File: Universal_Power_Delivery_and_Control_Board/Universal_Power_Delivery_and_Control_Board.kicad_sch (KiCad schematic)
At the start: 25 parts, among them SW2 TS1102-TD35HBM, U17 SN74LVC1G17DCKR, U19 TF-0803-0, U20 TCA9555PWR, U22 HC-PM254-8.5H-2X4PW-02A

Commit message: Fished layout for now, need to add some components for optional functionality.
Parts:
- removed C35, C36, C47: 100nF, Capacitor_SMD:C_0402_1005Metric_Pad0.74x0.62mm_HandSolder, symbol Device:C
- removed JP5, JP6: SolderJumper_3_Bridged12, Jumper:SolderJumper-3_P1.3mm_Bridged12_Pad1.0x1.5mm_NumberLabels, symbol Jumper:SolderJumper_3_Bridged12
- removed LED3: SK6812SIDE-A_C5378721, lcsc_footprints:C5378721_LED-SMD_4P-L4_0-W1_6-L, symbol lcsc_imported:SK6812SIDE-A_C5378721
- removed R29: 470R, Resistor_SMD:R_0402_1005Metric_Pad0.72x0.64mm_HandSolder, symbol Device:R
- removed R39: 100K, Resistor_SMD:R_0402_1005Metric_Pad0.72x0.64mm_HandSolder, symbol Device:R
- removed R40: 10K, Resistor_SMD:R_0402_1005Metric_Pad0.72x0.64mm_HandSolder, symbol Device:R
- removed SW2: TS1102-TD35HBM, lcsc_footprints:C36936640_SW-SMD_TS1102-TD35HBM, symbol lcsc_imported:TS1102-TD35HBM
- removed U17: SN74LVC1G17DCKR, lcsc_footprints:C10425_SC-70-5_L2_1-W1_3-P0_65-LS2_1-BR, symbol lcsc_imported:SN74LVC1G17DCKR
- added H1, H2, H3, H4: MountingHole_Pad, MountingHole:MountingHole_2.2mm_M2_Pad_Via, symbol Mechanical:MountingHole_Pad
- added R45: 33R, Resistor_SMD:R_0402_1005Metric_Pad0.72x0.64mm_HandSolder, symbol Device:R
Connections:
- net GND: now also U20.2 (A1), U20.3 (A2), H1.1, H2.1, H3.1, H4.1
- net P06: now reaches U20.10 (P06)
- net P07: now reaches U20.11 (P07)
- net at A1.5 (GPIO3): now also R45.2
- net PD_Section/IND_LED_DIN renamed UI_Section/IND_LED_DIN
- new net Button_LED_DIN: R45.1
- no-connect marks 9 -> 7
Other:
- added sheet UI_Section (UI_Section.kicad_sch)
- sheet PD_Section ports: added none; removed IND_LED_DIN, IND_LED_DOUT
- moved on the sheet: A1, C37, C38, C42, C43, R19, R20, R21, R25, R26, R30, U19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

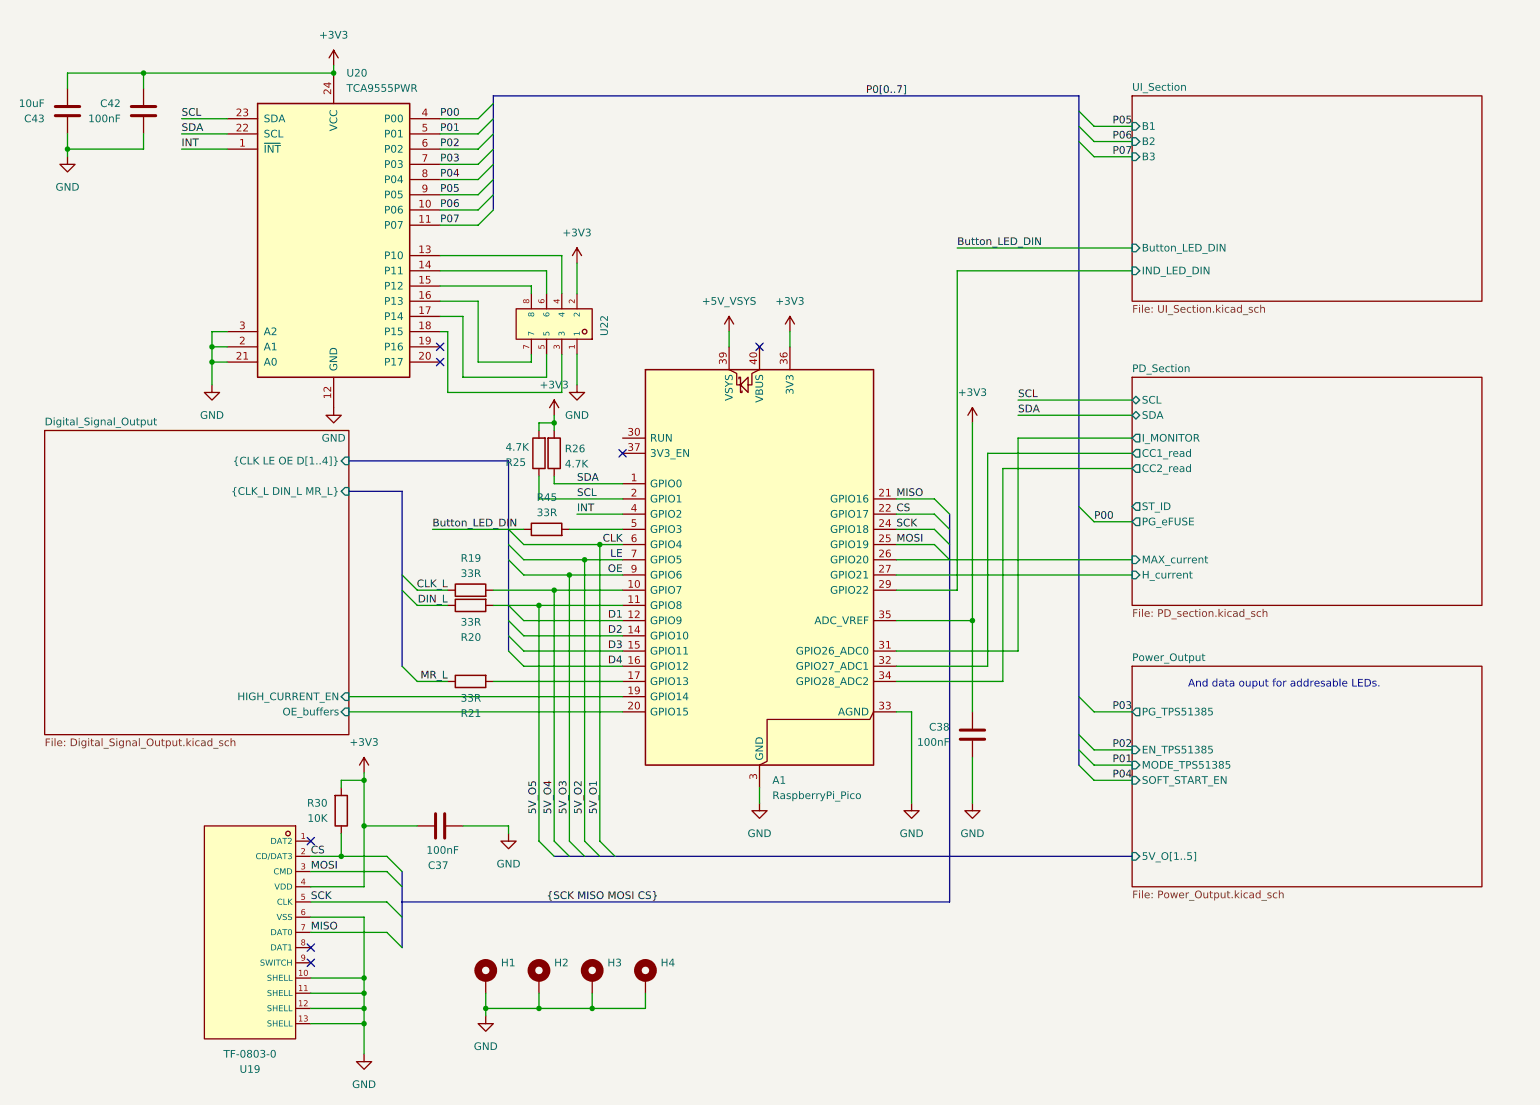
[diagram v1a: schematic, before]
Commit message: Finished layout 0 DRC errors.
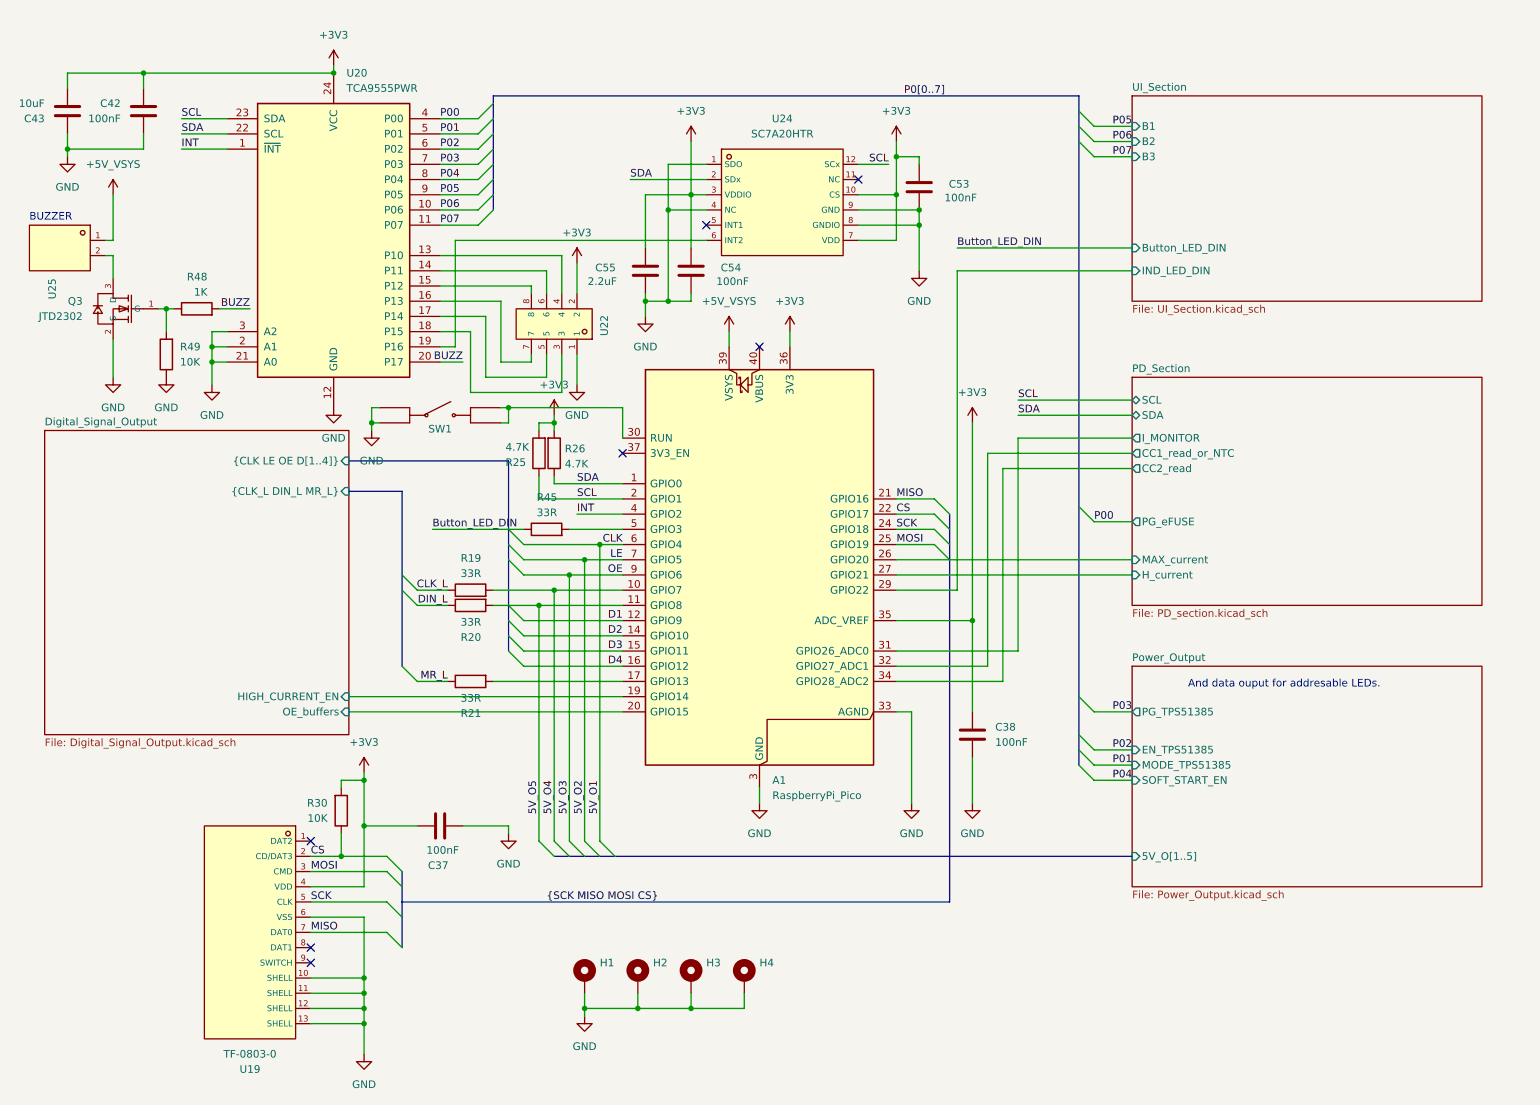
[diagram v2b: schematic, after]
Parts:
- added C53, C54: 100nF, Capacitor_SMD:C_0402_1005Metric_Pad0.74x0.62mm_HandSolder, symbol Device:C
- added C55: 2.2uF, Capacitor_SMD:C_0402_1005Metric_Pad0.74x0.62mm_HandSolder, symbol Device:C
- added Q3: JTD2302, lcsc_footprints:C42443455_SOT-23-3_L2_9-W1_5-P2_0-LS2_5-BR, symbol lcsc_imported:JTD2302
- added R48: 1K, Resistor_SMD:R_0402_1005Metric_Pad0.72x0.64mm_HandSolder, symbol Device:R
- added R49: 10K, Resistor_SMD:R_0402_1005Metric_Pad0.72x0.64mm_HandSolder, symbol Device:R
- added SW1: TSA016A2526A, lcsc_footprints:C2888428_SW-SMD_4P-L4_2-W3_3-P2_15-LS4_6, symbol lcsc_imported:TSA016A2526A
- added U24: SC7A20HTR, lcsc_footprints:C19274408_LGA-12_L2_0-W2_0-P0_50-TL, symbol lcsc_imported:SC7A20HTR
- added U25: S2B-ZR (LF)(SN), lcsc_footprints:C157930_CONN-TH_S2B-ZR-LF-SN, symbol lcsc_imported:S2B-ZR_(LF)(SN)
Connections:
- net +3V3: now also C53.2, C54.2, C55.2, U24.10 (CS), U24.3 (VDDIO), U24.7 (VDD)
- net +5V_VSYS: now also U25.1
- net GND: now also C53.1, C54.1, C55.1, Q3.2 (S), R49.1, SW1.1, SW1.2, U24.1 (SDO), U24.4 (NC), U24.8 (GNDIO), U24.9 (GND)
- net SCL: now also U24.12 (SCx)
- net SDA: now also U24.2 (SDx)
- net at U20.19 (P16): now also U24.6 (INT2)
- net BUZZ: now reaches U20.20 (P17)
- net BUZZ: now also R48.2
- net at A1.30 (RUN): now also SW1.3, SW1.4
- net PD_Section/CC1_read renamed PD_Section/CC1_read_or_NTC
- new net: Q3.1 (G), R48.1, R49.2
- new net: Q3.3 (D), U25.2
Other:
- sheet PD_Section ports: added CC1_read_or_NTC; removed CC1_read, ST_ID
- note added: "BUZZER"
- moved on the sheet: H1, H2, H3, H4

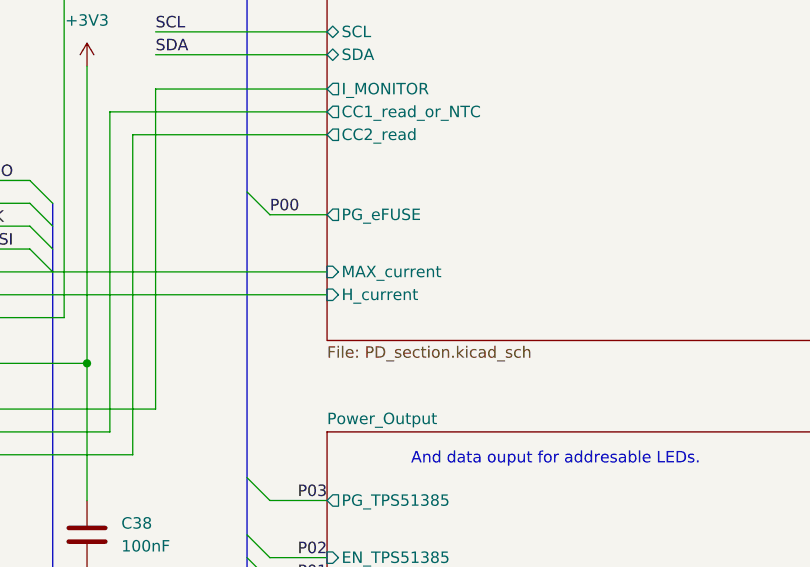
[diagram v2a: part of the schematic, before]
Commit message: Minor layout fixes to the UPDBC.
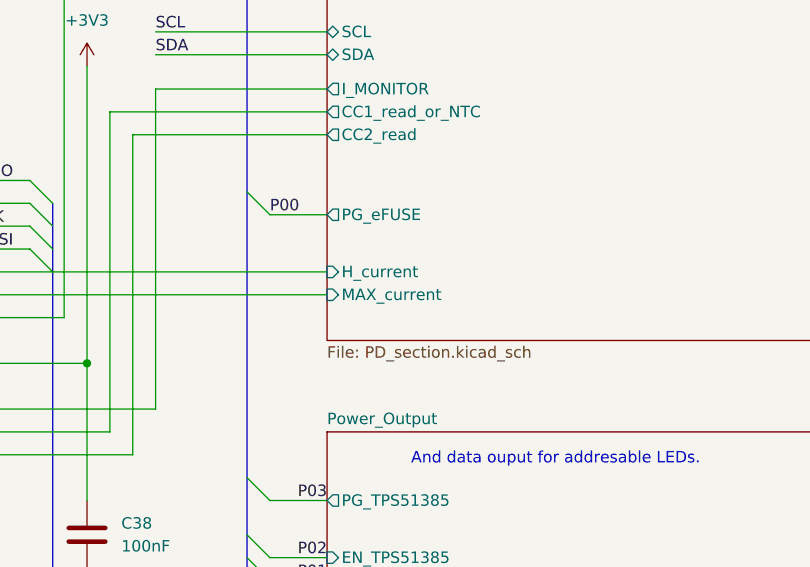
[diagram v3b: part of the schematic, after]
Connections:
- net PD_Section/H_current: now also A1.26 (GPIO20); no longer A1.27 (GPIO21)
- net PD_Section/MAX_current: now also A1.27 (GPIO21); no longer A1.26 (GPIO20)
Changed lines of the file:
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@@
 		)
 		(pin "H_current" input
-			(at 207.01 106.68 180)
+			(at 207.01 104.14 180)
 			(effects
 				(font
@@
 		)
 		(pin "MAX_current" input
-			(at 207.01 104.14 180)
+			(at 207.01 106.68 180)
 			(effects
 				(font

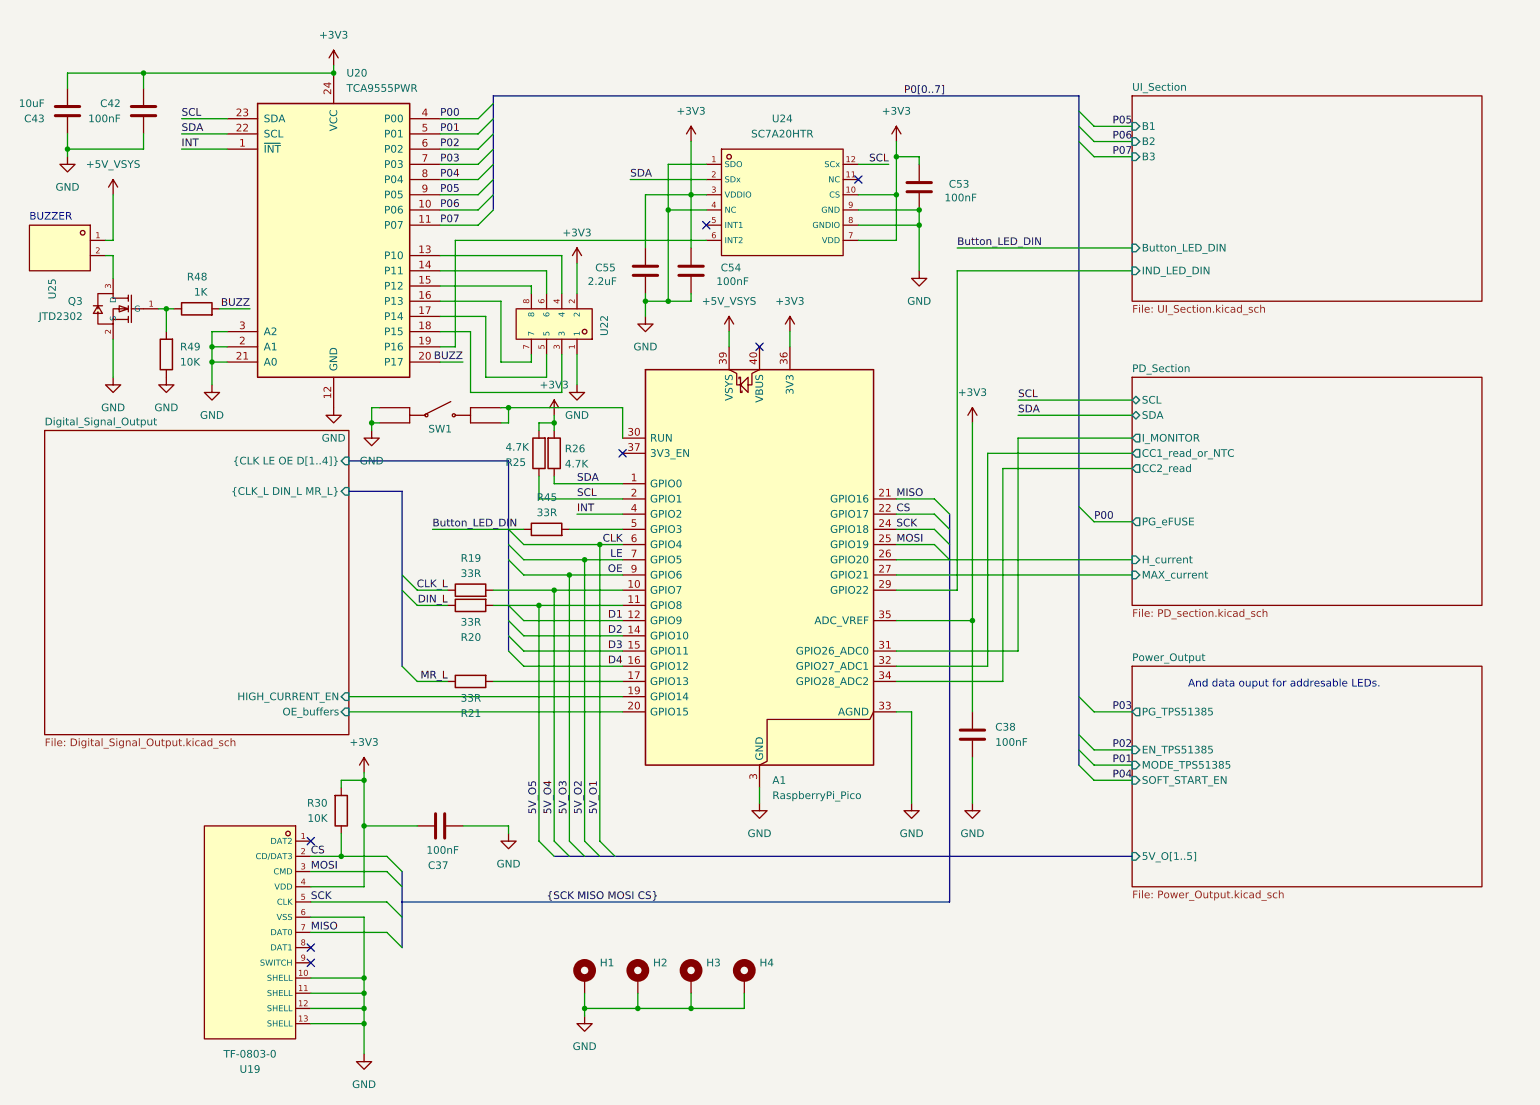
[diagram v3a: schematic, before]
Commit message: Small mostly cosmetic changes and reannotation of the schematic, followed by the export of the gerber files for production.
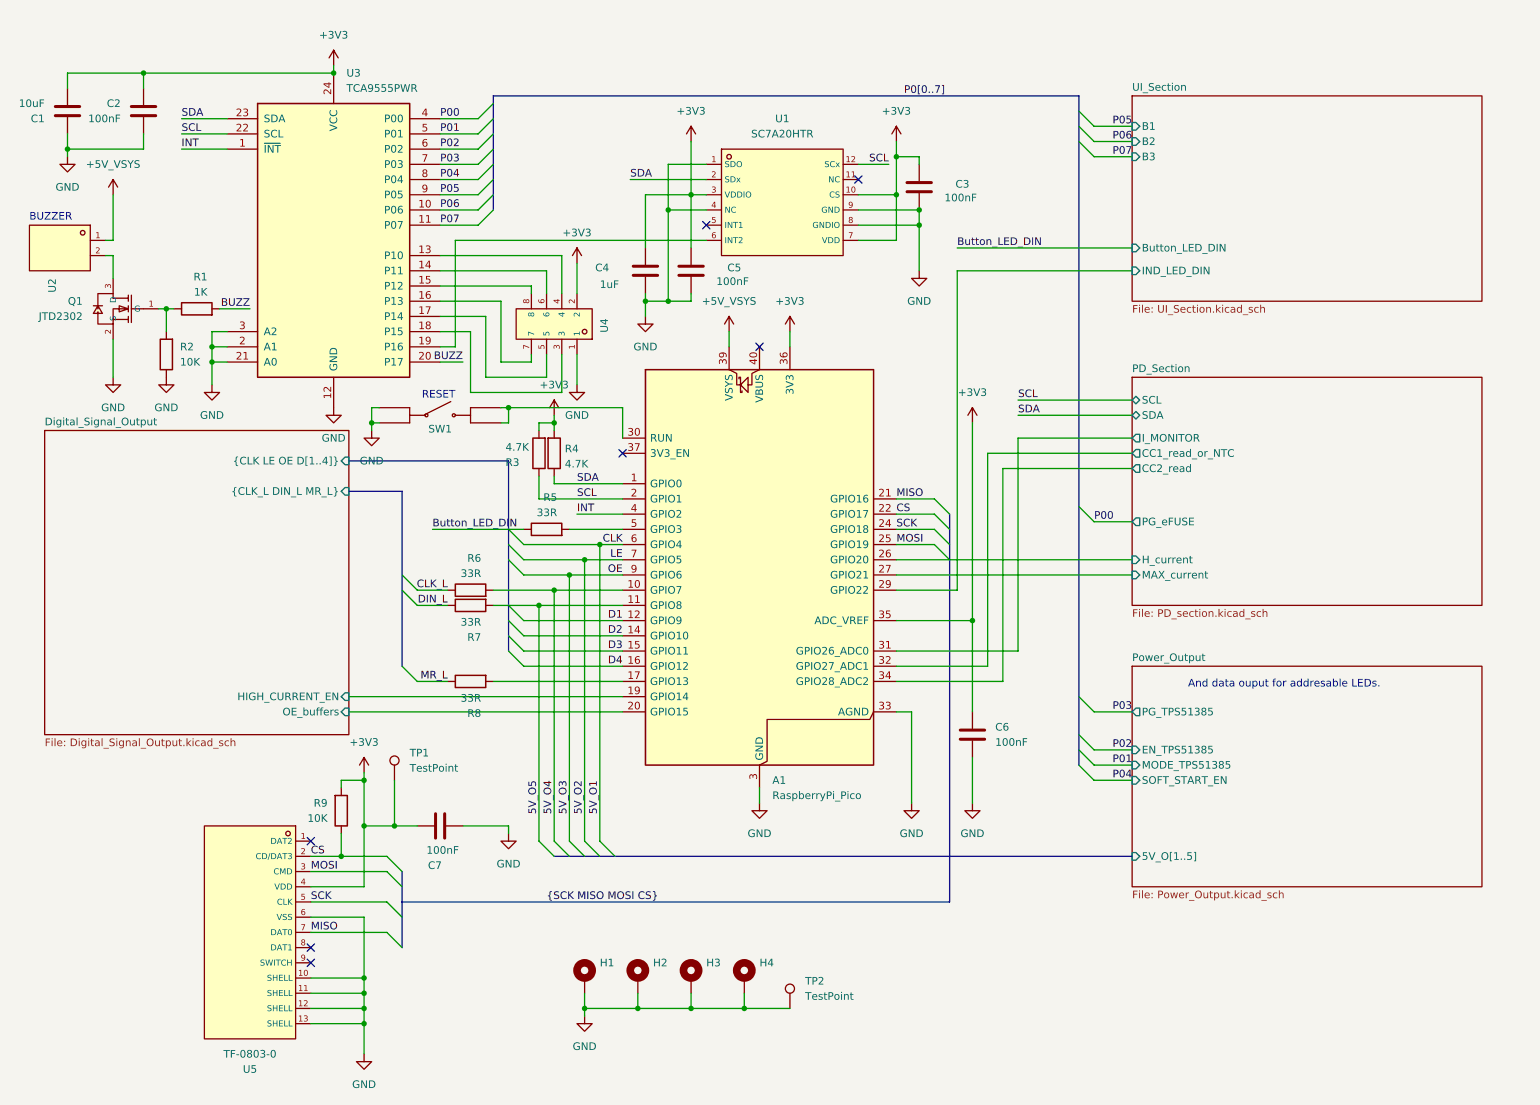
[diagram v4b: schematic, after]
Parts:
- added TP1, TP2: TestPoint, TestPoint:TestPoint_Pad_1.5x1.5mm, symbol Connector:TestPoint
- C4: renamed from C55; value 2.2uF -> 1uF
- renumbered C43 to C1, C42 to C2, C53 to C3, C54 to C5, C38 to C6, C37 to C7, Q3 to Q1, R48 to R1, R49 to R2, R25 to R3, R26 to R4, R45 to R5, R19 to R6, R20 to R7, R21 to R8, R30 to R9, U24 to U1, U25 to U2, U20 to U3, U22 to U4, U19 to U5
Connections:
- net +3V3: now also TP1.1
- net GND: now also TP2.1
- net SCL: now also U3.22 (SCL); no longer U3.23 (SDA)
- net SDA: now also U3.23 (SDA); no longer U3.22 (SCL)
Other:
- note added: "RESET"
- title: PD section -> Universal Power Delivery and Control Board

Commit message: Created design variant for 5x5x5 SC LED CUBEand added  interactive HTML BOM via plugin.
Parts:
- R3, R4: now not fitted
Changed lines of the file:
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@@
 		(on_board yes)
 		(in_pos_files yes)
-		(dnp no)
+		(dnp yes)
 		(property "Reference" "R4"
 			(at 112.268 85.5979 0)
@@
 		(on_board yes)
 		(in_pos_files yes)
-		(dnp no)
+		(dnp yes)
 		(property "Reference" "R3"
 			(at 102.362 87.8841 0)
